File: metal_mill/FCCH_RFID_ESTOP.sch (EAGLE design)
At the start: 29 parts, among them Q1 2N3906, Q2 2N3906, Q3 2N3906, Q4 2N3565, Q5 2N3565

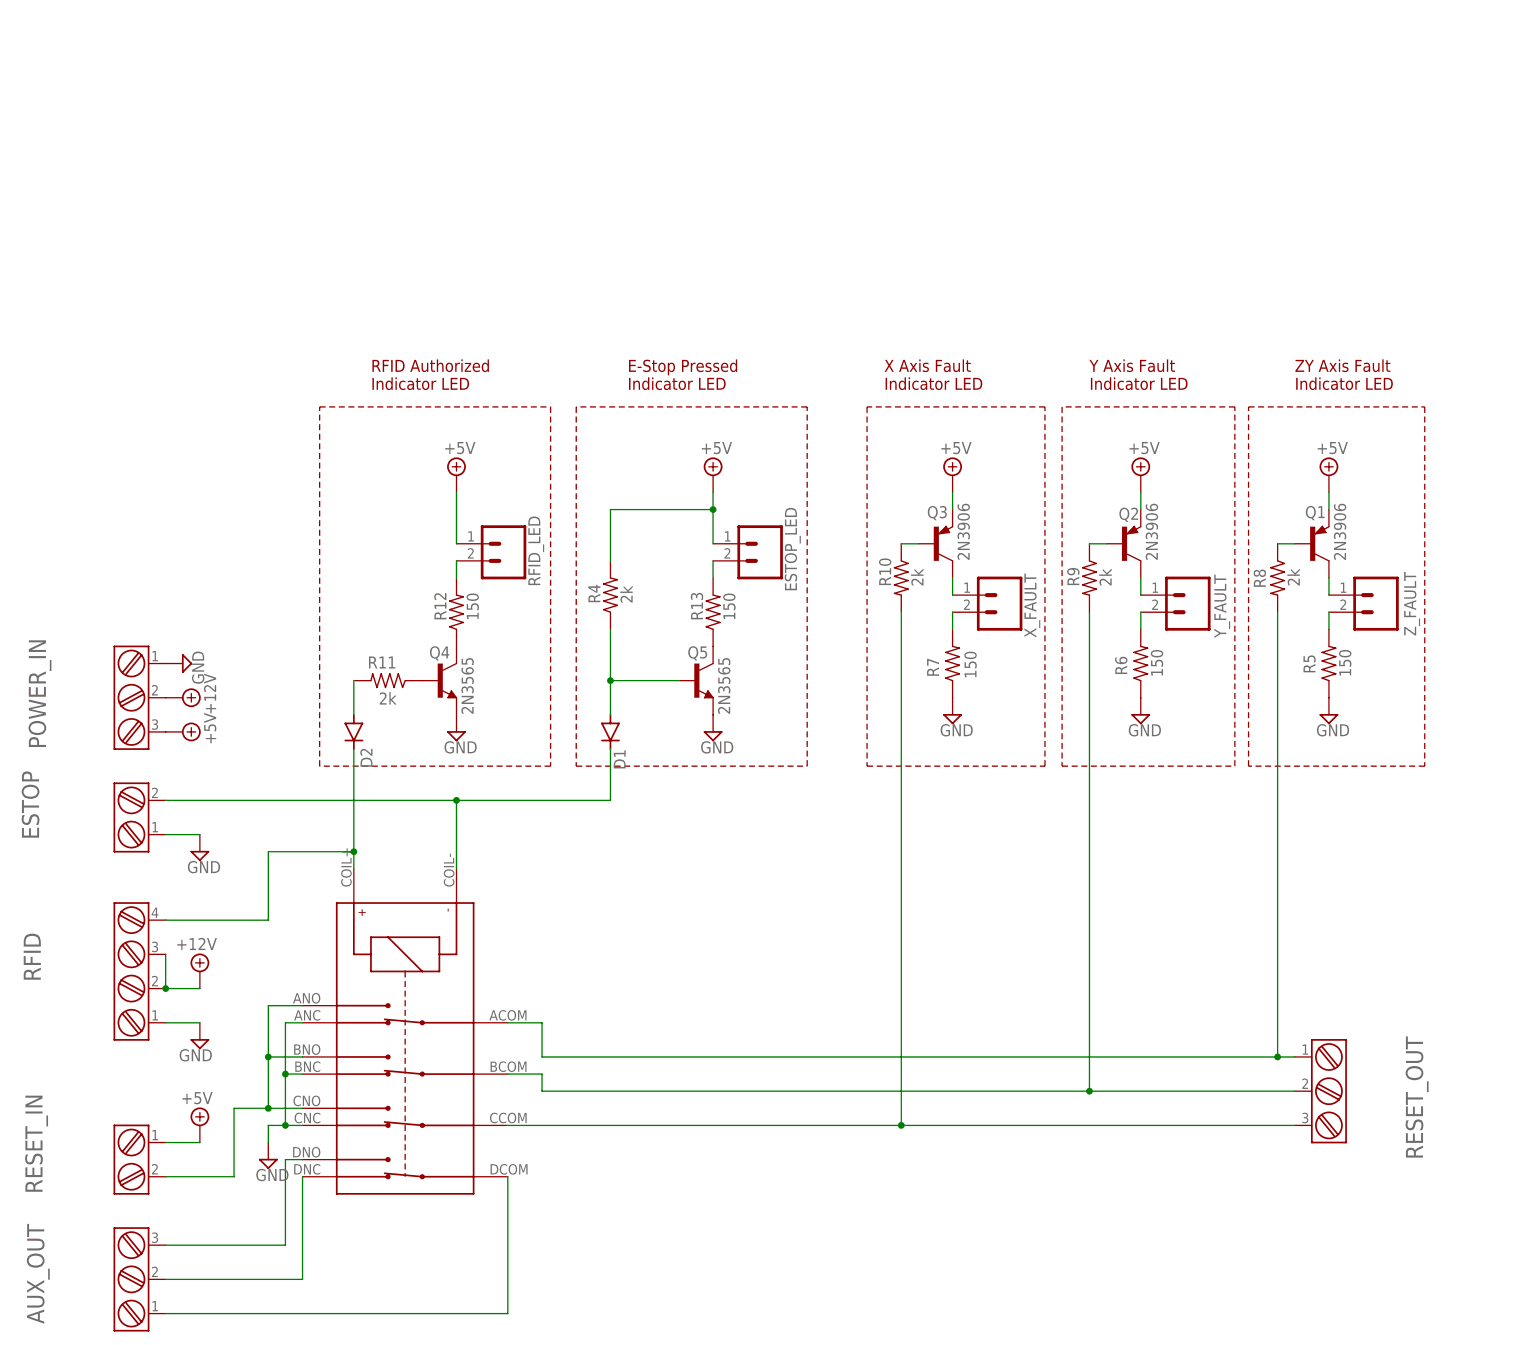
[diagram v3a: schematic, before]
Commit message: fixed some mistakes found by prototyping on a breadboard. * moved wire terminals to the end of the board * updated LED devices (was using a header) * updated resistor values
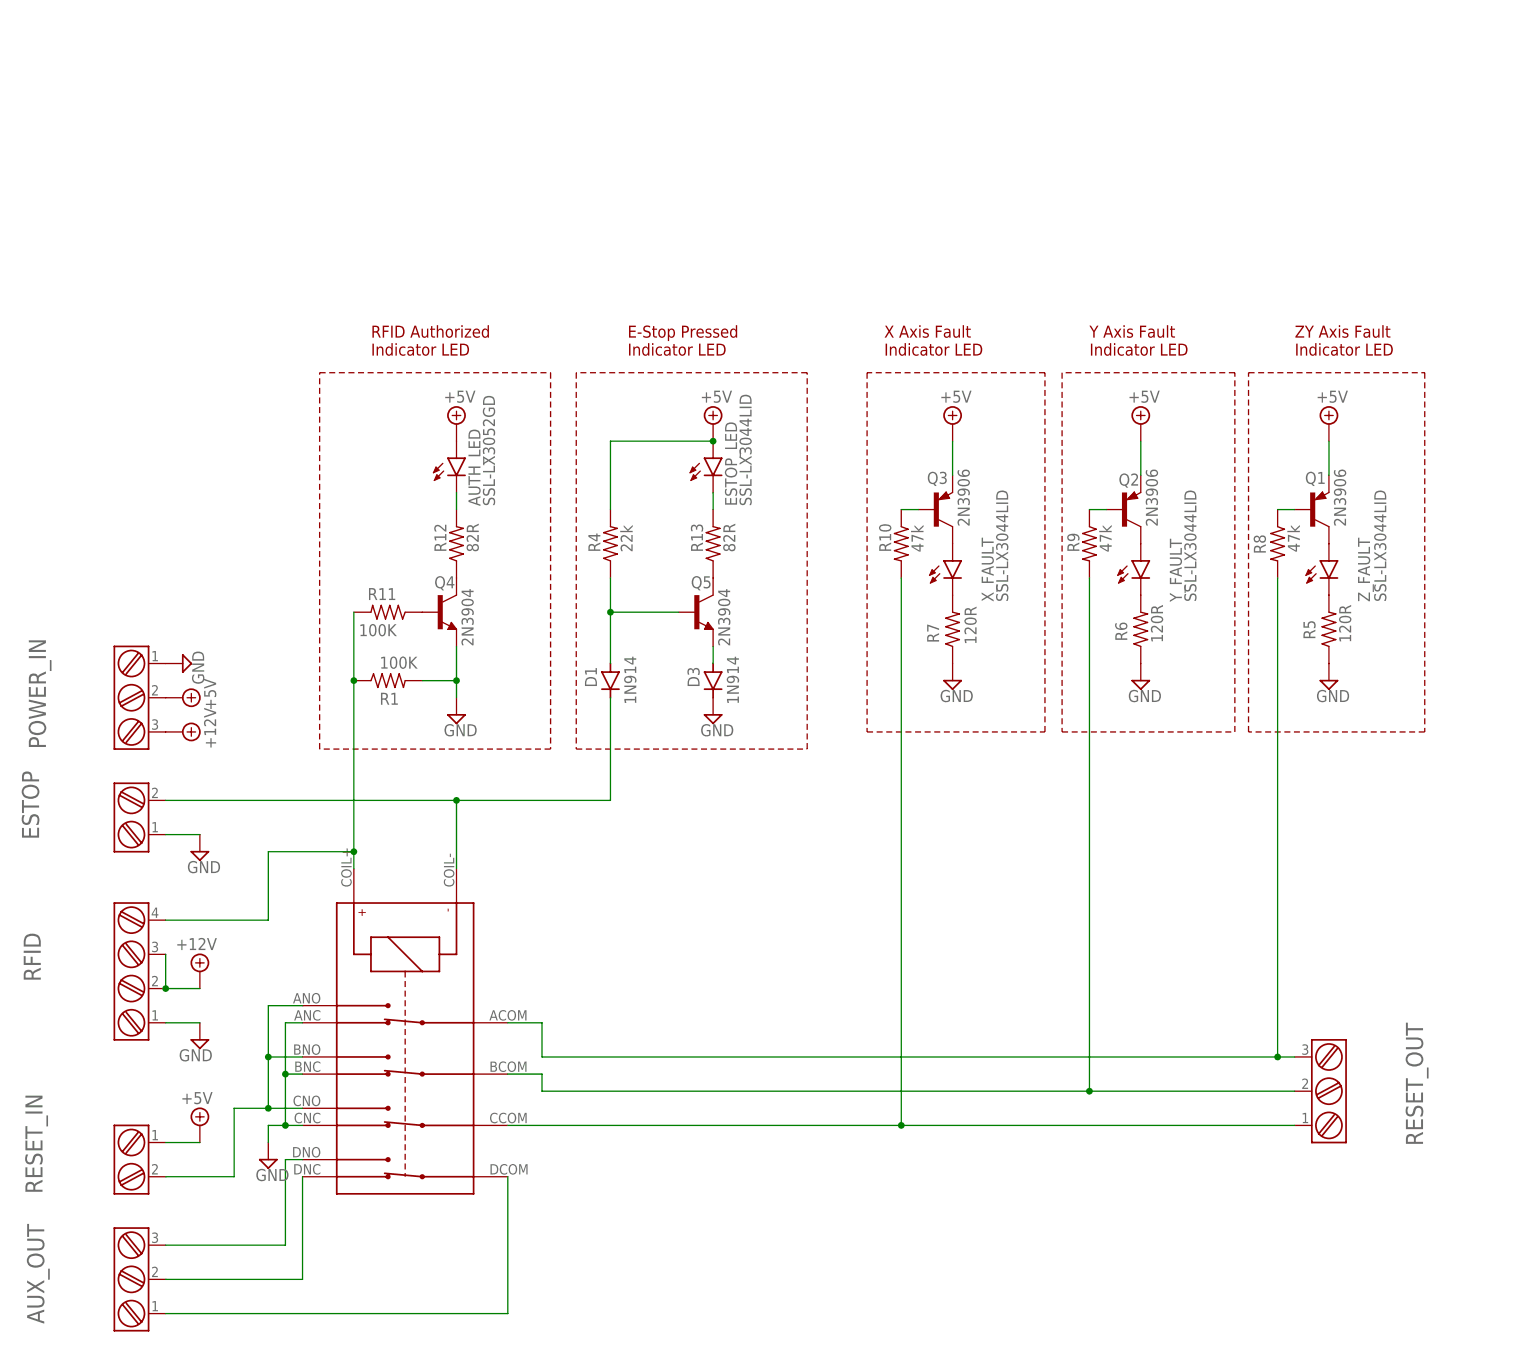
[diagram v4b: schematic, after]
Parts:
- removed D2: (no value), diode:DIODE-D-5
- removed RFID_LED: (no value), con-amp-quick:M02
- added AUTH_LED: SSL-LX3052GD, led:LED3MM
- added D3: 1N914, diode:DIODE-D-5
- added R1: 100K, rcl:R-US_0204/7
- D1: value (none) -> 1N914
- ESTOP_LED, X_FAULT, Y_FAULT, Z_FAULT: value (none) -> SSL-LX3044LID; device con-amp-quick:M02 -> led:LED3MM
- Q4, Q5: value 2N3565 -> 2N3904; device transistor-npn:2N3565 -> transistor-npn:2N3904
- R10, R8, R9: value 2k -> 47k
- R11: value 2k -> 100K
- R12, R13: value 150 -> 82R
- R4: value 2k -> 22k
- R5, R6, R7: value 150 -> 120R
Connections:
- removed net N$19: Q3.C, X_FAULT.1
- removed net N$21: R7.2, X_FAULT.2
- removed net N$23: Q2.C, Y_FAULT.1
- removed net N$25: R6.2, Y_FAULT.2
- removed net N$26: Q1.C, Z_FAULT.1
- removed net N$27: R5.2, Z_FAULT.2
- new net N$10: Q2.C, Y_FAULT.A
- new net N$11: R5.2, Z_FAULT.C
- new net N$12: Q1.C, Z_FAULT.A
- new net N$7: D3.A, Q5.E
- new net N$8: Q3.C, X_FAULT.A
- new net N$9: R6.2, Y_FAULT.C
- net +12V: now also POWER_IN.3; no longer POWER_IN.2
- net +5V: now also AUTH_LED.A, ESTOP_LED.A, POWER_IN.2; no longer ESTOP_LED.1, POWER_IN.3, RFID_LED.1
- net GND: now also D3.C, R1.2; no longer Q5.E
- net N$1: now also R7.2, X_FAULT.C; no longer D2.A, R11.2
- net N$15: now also ESTOP_LED.C; no longer ESTOP_LED.2
- net N$17: now also AUTH_LED.C; no longer RFID_LED.2
- net RFID_ENABLE: now also R1.1, R11.2; no longer D2.C
- net X_ERR/RES: now also RESET_OUT.1; no longer RESET_OUT.3
- net Z_ERR/RES: now also RESET_OUT.3; no longer RESET_OUT.1
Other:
- moved on the sheet: D1, Q1, Q2, Q3, R10, R11, R12, R13, R4, R5, R6, R7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
